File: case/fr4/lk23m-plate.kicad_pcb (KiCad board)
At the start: 2 copper layers, 76.2 x 119.1 mm, 8 parts

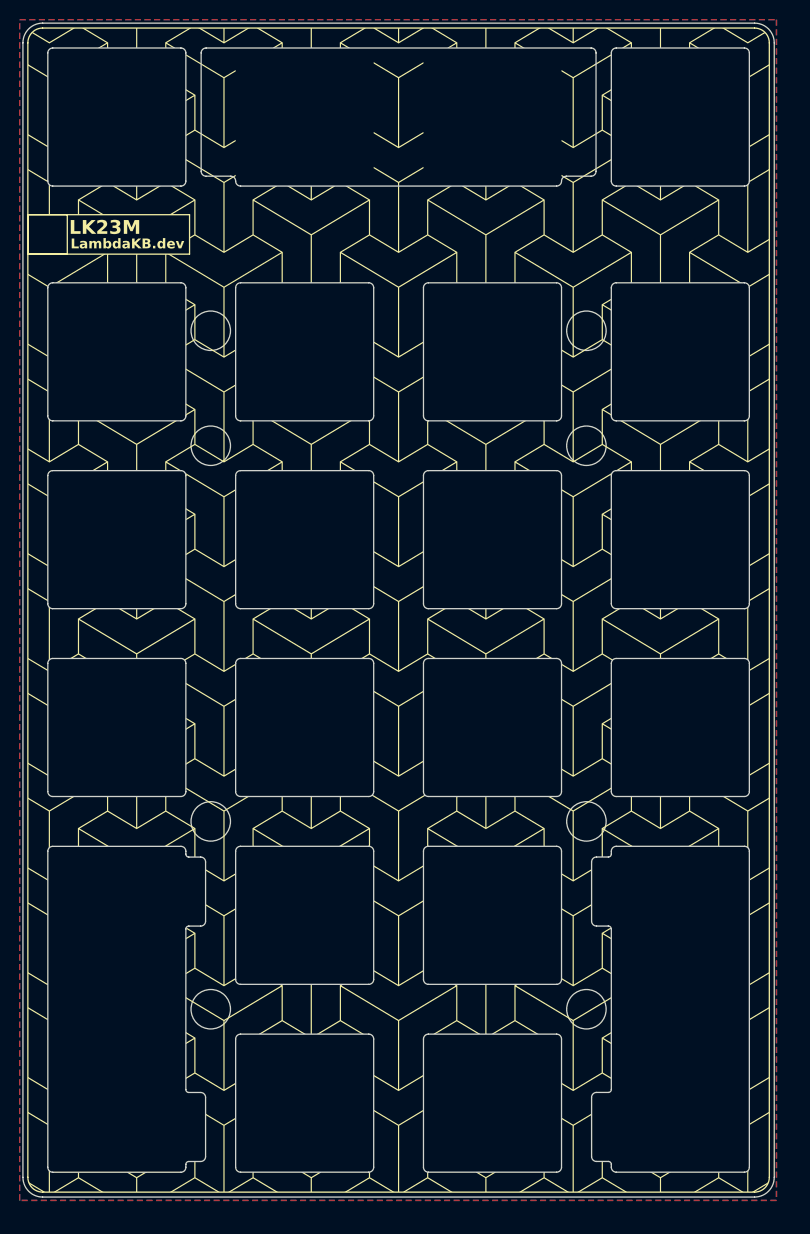
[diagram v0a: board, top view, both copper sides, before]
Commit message: Fix reset switch position in FR4 case
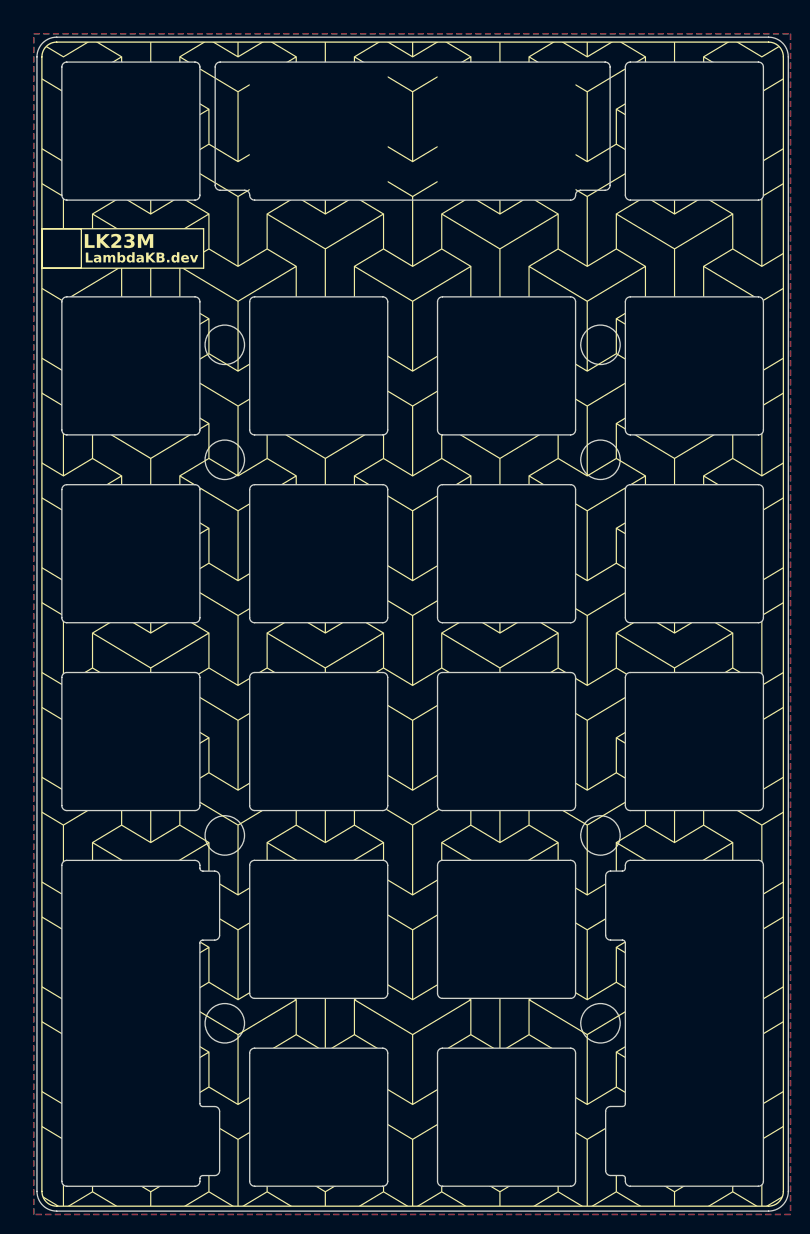
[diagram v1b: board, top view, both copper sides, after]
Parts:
- moved H4 2.02 mm to (87.2, 111.0)
- moved H5 2.02 mm to (87.2, 61.2)
- moved H2 2.02 mm to (87.2, 72.9)
- moved H8 2.02 mm to (49.0, 111.0)
- moved H1 2.02 mm to (49.0, 61.2)
- moved H6 2.02 mm to (49.0, 72.9)
- moved H7 2.02 mm to (87.2, 130.0)
- moved H3 2.02 mm to (49.0, 130.0)

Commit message: Upgrade project to KiCad 9 & cleanup FR4 plate pattern (#7)
* Upgrade KiBot to use KiCad 9
* Upgrade project to KiCad 9 & cleanup FR4 plate pattern
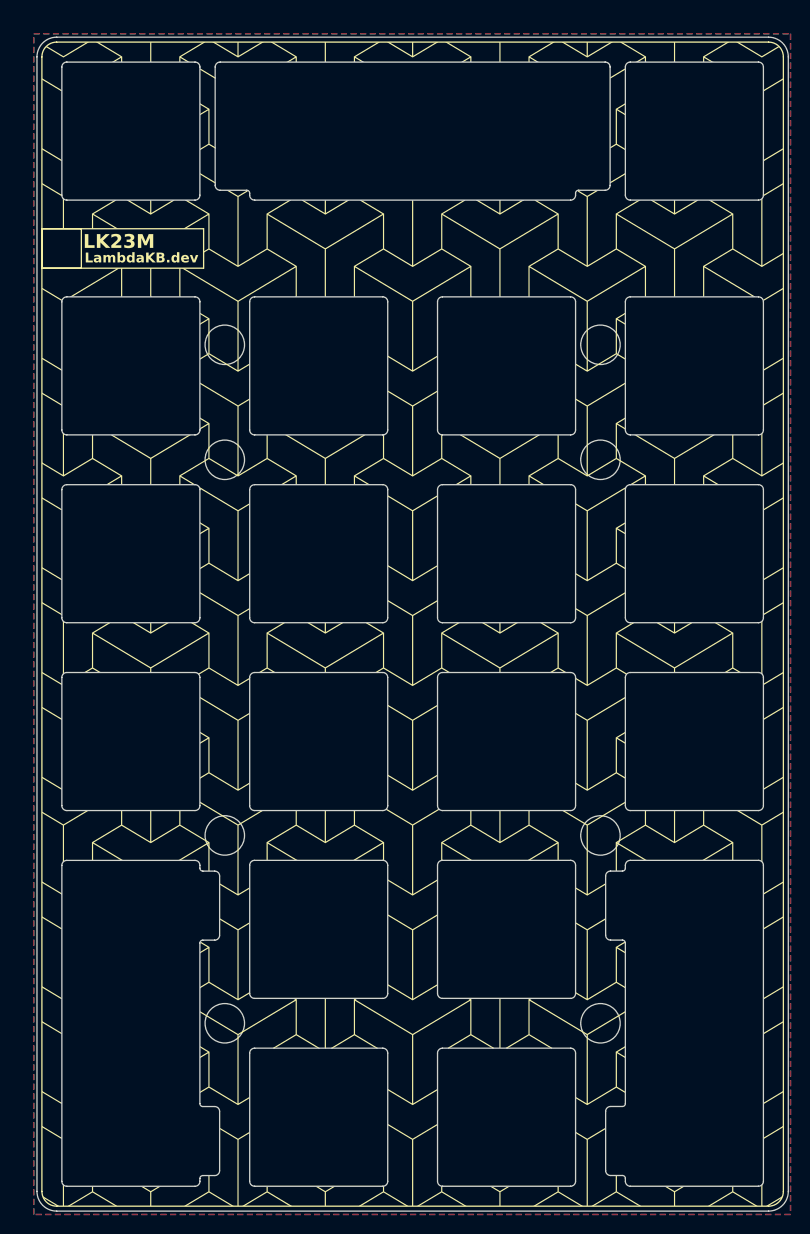
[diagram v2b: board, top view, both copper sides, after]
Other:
- outline, holes or cut-outs redrawn
